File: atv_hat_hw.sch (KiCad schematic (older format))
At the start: 51 parts, among them J1 GPIO_CONNECTOR, J10 conn_01x02_labeled, J11 conn_01x02_labeled, J12 conn_01x02_labeled, J2 conn_01x02_labeled, J3 conn_01x02_labeled, J4 conn_01x02_labeled, J5 conn_01x02_labeled, J6 conn_01x02_labeled, J7 enc28j60_hanrun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

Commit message: plus board ready for routing
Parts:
- removed D7, D8: Green, LED_SMD:LED_1206_3216Metric_Pad1.42x1.75mm_HandSolder, symbol Device:LED
- removed J10, J11, J12, J2, J3, J5, J6, J8, J9: conn_01x02_labeled, lib:SolderWirePad_1x02_P5.08mm_Drill1.5mm_labeled, symbol atv_cluster_hat:conn_01x02_labeled
- removed J4: conn_01x02_labeled, Connector_Wire:SolderWirePad_1x02_P7.62mm_Drill2.5mm, symbol atv_cluster_hat:conn_01x02_labeled
- removed J7: enc28j60_hanrun, lib:enc28j60_hanrun, symbol atv_cluster_hat:enc28j60_hanrun
- removed Q1, Q2, Q3, Q4, Q5, Q6, Q7, Q8, Q9: Q_NMOS_GDS, lib:SOT230P700X180-3N, symbol Device:Q_NMOS_GDS
- removed R1, R10, R2, R4, R5, R6, R7, R8, R9: 10k, Resistor_SMD:R_1206_3216Metric_Pad1.42x1.75mm_HandSolder, symbol Device:R
- removed R11, R12, R13, R14, R15, R16: 220, Resistor_SMD:R_1206_3216Metric_Pad1.42x1.75mm_HandSolder, symbol Device:R
- added J64: phoenix_1935161, lib:SolderWirePad_1x02_P9.0mm_Drill4.5mm, symbol atv_cluster_hat:phoenix_1935161
- added R65, R66: 10k, Resistor_SMD:R_1206_3216Metric_Pad1.42x1.75mm_HandSolder, symbol Device:R
- added R67, R68, R69, R70: 220, Resistor_SMD:R_1206_3216Metric_Pad1.42x1.75mm_HandSolder, symbol Device:R
- renumbered D2 to D1, D1 to D2, J1 to J65, R3 to R64
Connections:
- net +3V3: now also R65.2, R66.2
- net +5V: now also J64.2 (Pin_2)
- net GND: now also J64.1 (Pin_1)
- net GPIO12: now also R67.1
- net GPIO16: now also R68.1
- net GPIO20: now also R69.1
- net GPIO21: now also R70.1
- net at D3.2 (A): now also R67.2
- net at D4.2 (A): now also R68.2
- net at D5.2 (A): now also R69.2
- net at D6.2 (A): now also R70.2
- net ATV0_CTRL renamed GPIO22_GEN3
- net ATV1_CTRL renamed GPIO5
- net ATV2_CTRL renamed GPIO6
- net ATV3_CTRL renamed GPIO13
- net ATV4_CTRL renamed GPIO19
- net ATV5_CTRL renamed GPIO26
- net FAN0_PWM renamed GPIO4_GPIO_GCLK
- net FAN1_PWM renamed GPIO17_GEN0
- net FAN2_PWM renamed GPIO27_GEN2
- net GPIO2_SDA1 renamed SDA
- net SDA: now also R66.1
- net GPIO3_SCL1 renamed SCL
- net SCL: now also R65.1
- no-connect marks 13 -> 5
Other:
- note added: "GPIO/LED nets are managed globally"
- note removed: "Pinout is female and mirrored from \nboard connector"
- note removed: "https://raspi.tv/2015/ethernet-on-pi-zero-how-to-put-an-ethernet-port-on-your-pi"

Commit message: 64 port hat
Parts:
- removed H3, H4: MountingHole, lib:MountingHole_2.7mm_M2.5_uHAT_RPi, symbol Mechanical:MountingHole
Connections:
- net GPIO12: no longer R67.1
- net GPIO16: no longer R68.1
- net GPIO17_GEN0: now also R70.1
- net GPIO19: now also R68.1
- net GPIO20: no longer R69.1
- net GPIO21: now also R67.1; no longer R70.1
- net GPIO22_GEN3: now also R69.1
- net GPIO13 renamed GPIO_RST_1
- net GPIO18_GEN1 renamed GPIO_RST_3
- net GPIO26 renamed GPIO_RST_0
- net GPIO27_GEN2 renamed GPIO_RST_2
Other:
- moved on the sheet: D3, D4, D5, D6, R67, R68, R69, R70

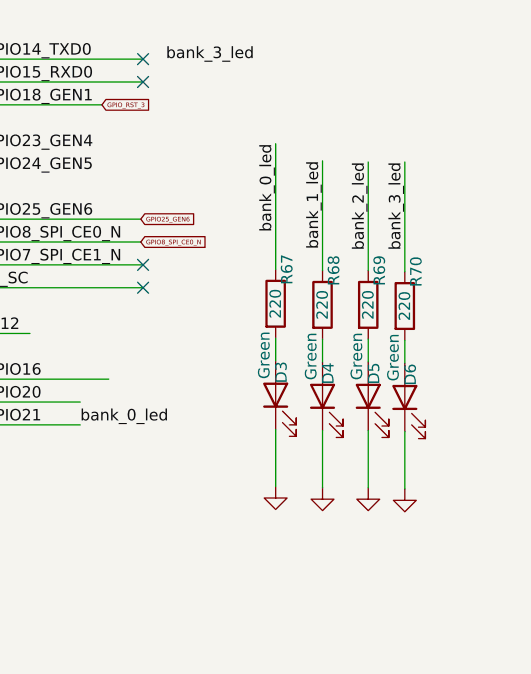
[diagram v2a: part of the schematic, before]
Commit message: PCB routed for 48 ports
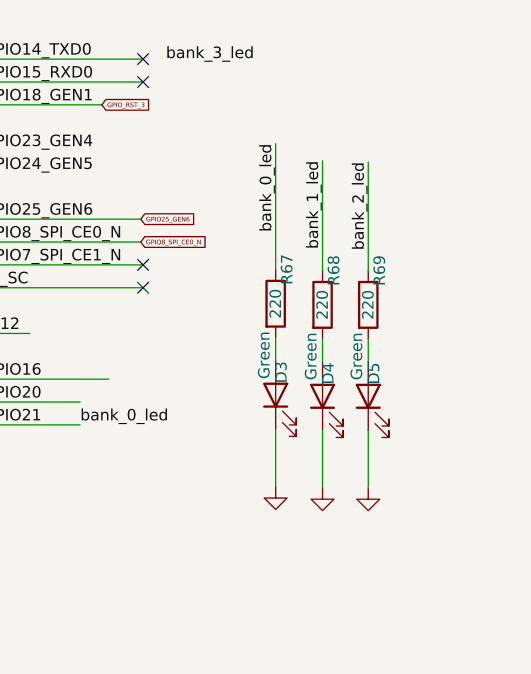
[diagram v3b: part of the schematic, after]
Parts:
- removed D6: Green, LED_SMD:LED_1206_3216Metric_Pad1.42x1.75mm_HandSolder, symbol Device:LED
- removed R70: 220, Resistor_SMD:R_1206_3216Metric_Pad1.42x1.75mm_HandSolder, symbol Device:R
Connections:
- wire segments 100 -> 97
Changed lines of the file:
@@
 GPIO21
-Wire Wire Line
-	10395 3430 10395 3680
 Wire Wire Line
 	10035 3425 10035 3675
 Wire Wire Line
 	9830 3420 9830 3670
-$Comp
-L Device:R R?
-U 1 1 5F0A71E8
-P 10395 2880
-AR Path="/5F028404/5F0A71E8" Ref="R?"  Part="1"
-AR Path="/5F0A71E8" Ref="R70"  Part="1"
-F 0 "R70" V 10445 3030 50  0000 C CNN
-F 1 "220" V 10395 2880 50  0000 C CNN
-F 2 "Resistor_SMD:R_1206_3216Metric_Pad1.42x1.75mm_HandSolder" V 10325 2880 50  0001 C CNN
-F 3 "~" H 10395 2880 50  0001 C CNN
-F 4 "P220ECT-ND" V 10395 2880 50  0001 C CNN "DPN"
-	1    10395 2880
-	1    0    0    -1
-$EndComp
-Wire Wire Line
-	10395 3030 10395 3130
-$Comp
-L Device:LED D?
-U 1 1 5F0A71E0
-P 10395 3280
-AR Path="/5F028404/5F0A71E0" Ref="D?"  Part="1"
-AR Path="/5F0A71E0" Ref="D6"  Part="1"
-F 0 "D6" H 10495 3255 50  0000 C CNN
-F 1 "Green" H 10570 3330 50  0000 C CNN
-F 2 "LED_SMD:LED_1206_3216Metric_Pad1.42x1.75mm_HandSolder" H 10395 3280 50  0001 C CNN
-F 3 "~" H 10395 3280 50  0001 C CNN
-F 4 "732-4990-1-ND" H 10395 3280 50  0001 C CNN "DPN"
-	1    10395 3280
-	0    -1   -1   0
-$EndComp
 $Comp
 L Device:R R?
@@
 Text Label 6640 2200 2    50   ~ 0
 bank_2_led
-Text Label 10395 2250 3    50   ~ 0
-bank_3_led
-Wire Wire Line
-	10395 2730 10395 2250
-$Comp
-L power:GND #PWR0254
-U 1 1 5F1A348A
-P 10395 3680
-F 0 "#PWR0254" H 10395 3430 50  0001 C CNN
-F 1 "GND" H 10400 3507 50  0001 C CNN
-F 2 "" H 10395 3680 50  0001 C CNN
-F 3 "" H 10395 3680 50  0001 C CNN
-	1    10395 3680
-	1    0    0    -1
-$EndComp
 Text Label 9350 1815 0    50   ~ 0
 bank_3_led
